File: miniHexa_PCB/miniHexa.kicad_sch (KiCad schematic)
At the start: 22 parts, among them SW1 SW_Push, U1 STM32F401RETx, Y2 25mhz

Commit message: start of version 2.0
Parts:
- removed R2: 0, Resistor_SMD:R_0603_1608Metric, symbol Device:R
- added U7: LSM6DS3, Package_LGA:LGA-14_3x2.5mm_P0.5mm_LayoutBorder3x4y, symbol Sensor_Motion:LSM6DS3
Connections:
- net +3.3V: now also U7.12 (CS), U7.5 (VDDIO), U7.8 (VDD)
- net GND: now also U7.1 (SDO/SA0), U7.2 (SDX), U7.3 (SCX), U7.6 (GND), U7.7 (GND)
- net RX: now reaches U1.42 (PA9)
- net TX: now reaches U1.43 (PA10)
- net at U1.61 (PB8): now also U7.13 (SCL)
- net I2C_SCK: no longer names the net of U1.58 (PB6)
- net I2C_SDA: no longer names the net of U1.59 (PB7)
- net I2C_SDA: now also U7.14 (SDA)
- net SERVO17: no longer names the net of U1.26 (PB0)
- net SERVO18: no longer names the net of U1.27 (PB1)

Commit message: mega update
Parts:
- added C31, C32, C33: 100nF, Capacitor_SMD:C_0402_1005Metric, symbol Device:C
- added R2, R6: 10k, Resistor_SMD:R_0402_1005Metric, symbol Device:R
- added R7: 0, Resistor_SMD:R_0603_1608Metric, symbol Device:R
- added U8: ST67W611M1A6UTR, pro_lib:U_QFN32L_ST67W611M1_STM-L, symbol pro_lib:ST67W611M1A6UTR
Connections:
- net +3.3V: now also C31.2, C32.2, C33.2, R2.1, R6.1, U8.16 (VDD33), U8.17 (CHIP_EN), U8.25 (VDDIO), U8.9 (VDDIO)
- net GND: now also C31.1, C32.1, C33.1, U8.10 (GND), U8.15 (GND), U8.18 (GND), U8.26 (GND), U8.30 (GND), U8.32 (GND), U8.33 (GND), U8.34 (GND), U8.35 (GND), U8.36 (GND)
- net ST67_BOOT: now reaches U1.17 (PA3)
- net ST67_BOOT: now also U8.3 (BOOT)
- net SP_CLK: now reaches U1.21 (PA5)
- net SP_CLK: now also U8.28 (SP_CLK)
- net at U1.22 (PA6): now also R7.2
- net SPI_MOSI: now reaches U1.23 (PA7)
- net SPI_MOSI: now also U8.27 (SPI_MOSI)
- net SPI_CS: now reaches U1.33 (PB12)
- net SPI_CS: now also U8.24 (SPI_CS)
- net ST67_TX: now reaches U1.38 (PC7)
- net ST67_TX: now also U8.22 (UART_TX)
- net SPI_RDY: now reaches U1.39 (PC8)
- net SPI_RDY: now also U8.21 (SPI_RDY)
- net SERVO_RX: now reaches U1.58 (PB6)
- net SERVO_RX: now also R2.2
- net at U7.14 (SDA): now also U1.61 (PB8); no longer U1.59 (PB7)
- net at U7.13 (SCL): now also U1.62 (PB9); no longer U1.61 (PB8)
- net CHIPEN_MIC_L renamed ST67_RX
- net ST67_RX: now also U8.23 (UART_RX)
- net CHIPEN_MIC_R: no longer names the net of U1.25 (PC5)
- net RX: no longer names the net of U1.42 (PA9)
- net TX: no longer names the net of U1.43 (PA10)
- new net SERVO_TX: R6.2, U1.59 (PB7)
- new net SPI_MISO: R7.1, U8.29 (SPI_MISO)
- no-connect marks 1 -> 3
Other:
- moved on the sheet: U7

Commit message: routed
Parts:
- C31, C32, C33: footprint Capacitor_SMD:C_0402_1005Metric -> Capacitor_SMD:C_0805_2012Metric
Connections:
- net +3.3V: no longer U8.17 (CHIP_EN)
- net CHIP_EN: now reaches U1.41 (PA8)
- net CHIP_EN: now also U8.17 (CHIP_EN)
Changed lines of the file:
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@@
 		)
 	)
+	(global_label "CHIP_EN"
+		(shape input)
+		(at 120.65 59.69 0)
+		(fields_autoplaced yes)
+		(effects
+			(font
+				(size 1.27 1.27)
+			)
+			(justify left)
+		)
+		(property "Intersheetrefs" "${INTERSHEET_REFS}"
+			(at 131.5576 59.69 0)
+			(hide yes)
+			(show_name no)
+			(do_not_autoplace no)
+			(effects
+				(font
+					(size 1.27 1.27)
+				)
+				(justify left)
+			)
+		)
+	)
 	(global_label "SPI_RDY"
 		(shape input)
@@
 		)
 	)
+	(global_label "CHIP_EN"
+		(shape input)
+		(at 175.26 71.12 180)
+		(fields_autoplaced yes)
+		(effects
+			(font
+				(size 1.27 1.27)
+			)
+			(justify right)
+		)
+		(property "Intersheetrefs" "${INTERSHEET_REFS}"
+			(at 164.3524 71.12 0)
+			(hide yes)
+			(show_name no)
+			(do_not_autoplace no)
+			(effects
+				(font
+					(size 1.27 1.27)
+				)
+				(justify right)
+			)
+		)
+	)
 	(symbol
 		(lib_id "power:GND")
@@
 		(lib_id "Device:C")
 		(at 261.62 54.61 0)
+		(mirror y)
 		(unit 1)
 		(body_style 1)
@@
 		(dnp no)
 		(property "Reference" "C33"
-			(at 253.746 50.038 0)
+			(at 269.494 50.038 0)
 			(show_name no)
 			(do_not_autoplace no)
@@
 		)
 		(property "Value" "100nF"
-			(at 253.746 52.578 0)
+			(at 269.494 52.578 0)
 			(show_name no)
 			(do_not_autoplace no)
@@
 			)
 		)
-		(property "Footprint" "Capacitor_SMD:C_0402_1005Metric"
-			(at 262.5852 58.42 0)
+		(property "Footprint" "Capacitor_SMD:C_0805_2012Metric"
+			(at 260.6548 58.42 0)
 			(hide yes)
 			(show_name no)
@@
 	)
 	(symbol
-		(lib_id "power:+3.3V")
-		(at 175.26 71.12 90)
-		(unit 1)
-		(body_style 1)
-		(exclude_from_sim no)
-		(in_bom yes)
-		(on_board yes)
-		(in_pos_files yes)
-		(dnp no)
-		(property "Reference" "#PWR069"
-			(at 179.07 71.12 0)
-			(hide yes)
-			(show_name no)
-			(do_not_autoplace no)
-			(effects
-				(font
-					(size 1.27 1.27)
-				)
-			)
-		)
-		(property "Value" "+3.3V"
-			(at 170.434 69.596 90)
-			(show_name no)
-			(do_not_autoplace no)
-			(effects
-				(font
-					(size 1.27 1.27)
-				)
-			)
-		)
-		(property "Footprint" ""
-			(at 175.26 71.12 0)
-			(hide yes)
-			(show_name no)
-			(do_not_autoplace no)
-			(effects
-				(font
-					(size 1.27 1.27)
-				)
-			)
-		)
-		(property "Datasheet" ""
-			(at 175.26 71.12 0)
-			(hide yes)
-			(show_name no)
-			(do_not_autoplace no)
-			(effects
-				(font
-					(size 1.27 1.27)
-				)
-			)
-		)
-		(property "Description" "Power symbol creates a global label with name \"+3.3V\""
-			(at 175.26 71.12 0)
-			(hide yes)
-			(show_name no)
-			(do_not_autoplace no)
-			(effects
-				(font
-					(size 1.27 1.27)
-				)
-			)
-		)
-		(pin "1"
-		)
-		(instances
-			(project "miniHexa"
-				(path "/3449ee66-2977-4802-a474-0821cdf4e79b"
-					(reference "#PWR069")
-					(unit 1)
-				)
-			)
-		)
-	)
-	(symbol
 		(lib_id "Device:C")
 		(at 52.07 24.13 0)
@@
 			)
 		)
-		(property "Footprint" "Capacitor_SMD:C_0402_1005Metric"
+		(property "Footprint" "Capacitor_SMD:C_0805_2012Metric"
 			(at 160.9852 68.58 0)
 			(hide yes)
@@
 			)
 		)
-		(property "Footprint" "Capacitor_SMD:C_0402_1005Metric"
+		(property "Footprint" "Capacitor_SMD:C_0805_2012Metric"
 			(at 167.3352 50.8 0)
 			(hide yes)

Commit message: update
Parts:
- added C34, C35: 100nF, Capacitor_SMD:C_0402_1005Metric, symbol Device:C
- added R8, R9: 4.7k, Resistor_SMD:R_0402_1005Metric, symbol Device:R
- U7: value LSM6DS3 -> LSM6DSL
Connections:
- net +3.3V: now also C34.2, C35.2, R8.2, R9.2
- net GND: now also C34.1, C35.1
- net IMU_INT1: now reaches U1.40 (PC9)
- net IMU_INT1: now also U7.4 (INT1)
- net at U1.61 (PB8): now also U7.13 (SCL), R8.1; no longer U7.14 (SDA)
- net at U1.62 (PB9): now also U7.14 (SDA), R9.1; no longer U7.13 (SCL)

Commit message: fixed RESET button issue
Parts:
- C1: value 20uF -> 2.2uF
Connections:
- net GND: now also C13.1, SW1.1; no longer C13.2
- net NRST: now reaches R1.1
- net NRST: now also C13.2, SW1.2, U1.7 (NRST); no longer SW1.1
- net SWDIO: now reaches U1.46 (PA13)
- net SWCLK: now reaches U1.49 (PA14)
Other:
- note added: "RESET BUTTON"
- moved on the sheet: C28, C29, R3

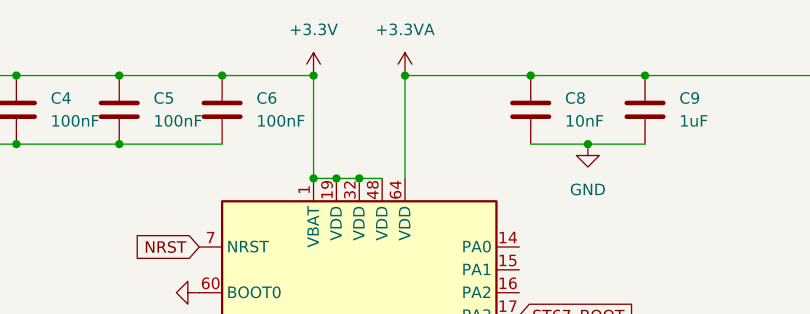
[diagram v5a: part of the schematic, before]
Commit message: updated some power lines
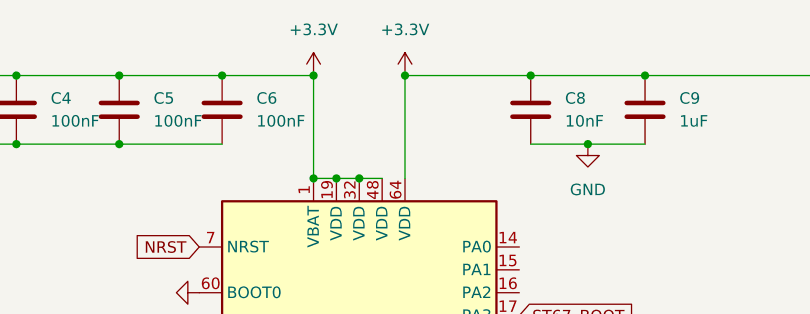
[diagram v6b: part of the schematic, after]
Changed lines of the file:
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@@
 	)
 	(junction
-		(at 107.95 20.32)
-		(diameter 0)
-		(color 0 0 0 0)
-	)
-	(junction
 		(at 255.27 140.97)
 		(diameter 0)
@@
 	)
 	(junction
+		(at 107.95 20.32)
+		(diameter 0)
+		(color 0 0 0 0)
+	)
+	(junction
 		(at 133.35 100.33)
 		(diameter 0)
@@
 	)
 	(symbol
-		(lib_id "power:+3.3VA")
-		(at 107.95 20.32 0)
-		(unit 1)
-		(body_style 1)
-		(exclude_from_sim no)
-		(in_bom yes)
-		(on_board yes)
-		(in_pos_files yes)
-		(dnp no)
-		(fields_autoplaced yes)
-		(property "Reference" "#PWR016"
-			(at 107.95 24.13 0)
-			(hide yes)
-			(show_name no)
-			(do_not_autoplace no)
-			(effects
-				(font
-					(size 1.27 1.27)
-				)
-			)
-		)
-		(property "Value" "+3.3VA"
-			(at 107.95 15.24 0)
-			(show_name no)
-			(do_not_autoplace no)
-			(effects
-				(font
-					(size 1.27 1.27)
-				)
-			)
-		)
-		(property "Footprint" ""
-			(at 107.95 20.32 0)
-			(hide yes)
-			(show_name no)
-			(do_not_autoplace no)
-			(effects
-				(font
-					(size 1.27 1.27)
-				)
-			)
-		)
-		(property "Datasheet" ""
-			(at 107.95 20.32 0)
-			(hide yes)
-			(show_name no)
-			(do_not_autoplace no)
-			(effects
-				(font
-					(size 1.27 1.27)
-				)
-			)
-		)
-		(property "Description" "Power symbol creates a global label with name \"+3.3VA\""
-			(at 107.95 20.32 0)
-			(hide yes)
-			(show_name no)
-			(do_not_autoplace no)
-			(effects
-				(font
-					(size 1.27 1.27)
-				)
-			)
-		)
-		(pin "1"
-		)
-		(instances
-			(project "miniHexa"
-				(path "/3449ee66-2977-4802-a474-0821cdf4e79b"
-					(reference "#PWR016")
-					(unit 1)
-				)
-			)
-		)
-	)
-	(symbol
 		(lib_id "Device:C")
 		(at 223.52 88.9 180)
@@
 					(unit 1)
 				)
+			)
+		)
+	)
+	(symbol
+		(lib_id "power:+3.3V")
+		(at 107.95 20.32 0)
+		(unit 1)
+		(body_style 1)
+		(exclude_from_sim no)
+		(in_bom yes)
+		(on_board yes)
+		(in_pos_files yes)
+		(dnp no)
+		(fields_autoplaced yes)
+		(property "Reference" "#PWR016"
+			(at 107.95 24.13 0)
+			(hide yes)
+			(show_name no)
+			(do_not_autoplace no)
+			(effects
+				(font
+					(size 1.27 1.27)
+				)
+			)
+		)
+		(property "Value" "+3.3V"
+			(at 107.95 15.24 0)
+			(show_name no)
+			(do_not_autoplace no)
+			(effects
+				(font
+					(size 1.27 1.27)
+				)
+			)
+		)
+		(property "Footprint" ""
+			(at 107.95 20.32 0)
+			(hide yes)
+			(show_name no)
+			(do_not_autoplace no)
+			(effects
+				(font
+					(size 1.27 1.27)
+				)
+			)
+		)
+		(property "Datasheet" ""
+			(at 107.95 20.32 0)
+			(hide yes)
+			(show_name no)
+			(do_not_autoplace no)
+			(effects
+				(font
+					(size 1.27 1.27)
+				)
+			)
+		)
+		(property "Description" "Power symbol creates a global label with name \"+3.3V\""
+			(at 107.95 20.32 0)
+			(hide yes)
+			(show_name no)
+			(do_not_autoplace no)
+			(effects
+				(font
+					(size 1.27 1.27)
+				)
+			)
+		)
+		(pin "1"
+		)
+		(instances
+			(project "miniHexa"
+				(path "/3449ee66-2977-4802-a474-0821cdf4e79b"
+					(reference "#PWR016")
+					(unit 1)
+				)

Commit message: tried to make it cleaner
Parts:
- removed R3: 0, Resistor_SMD:R_0603_1608Metric, symbol Device:R
- added JP1: 0hm, Resistor_SMD:R_0603_1608Metric, symbol Jumper:Jumper_2_Bridged
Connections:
- net MIC_SCK: now also JP1.1 (A), JP1.2 (B)
- no-connect marks 3 -> 12
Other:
- moved on the sheet: C34, C35, R32, R8, R9

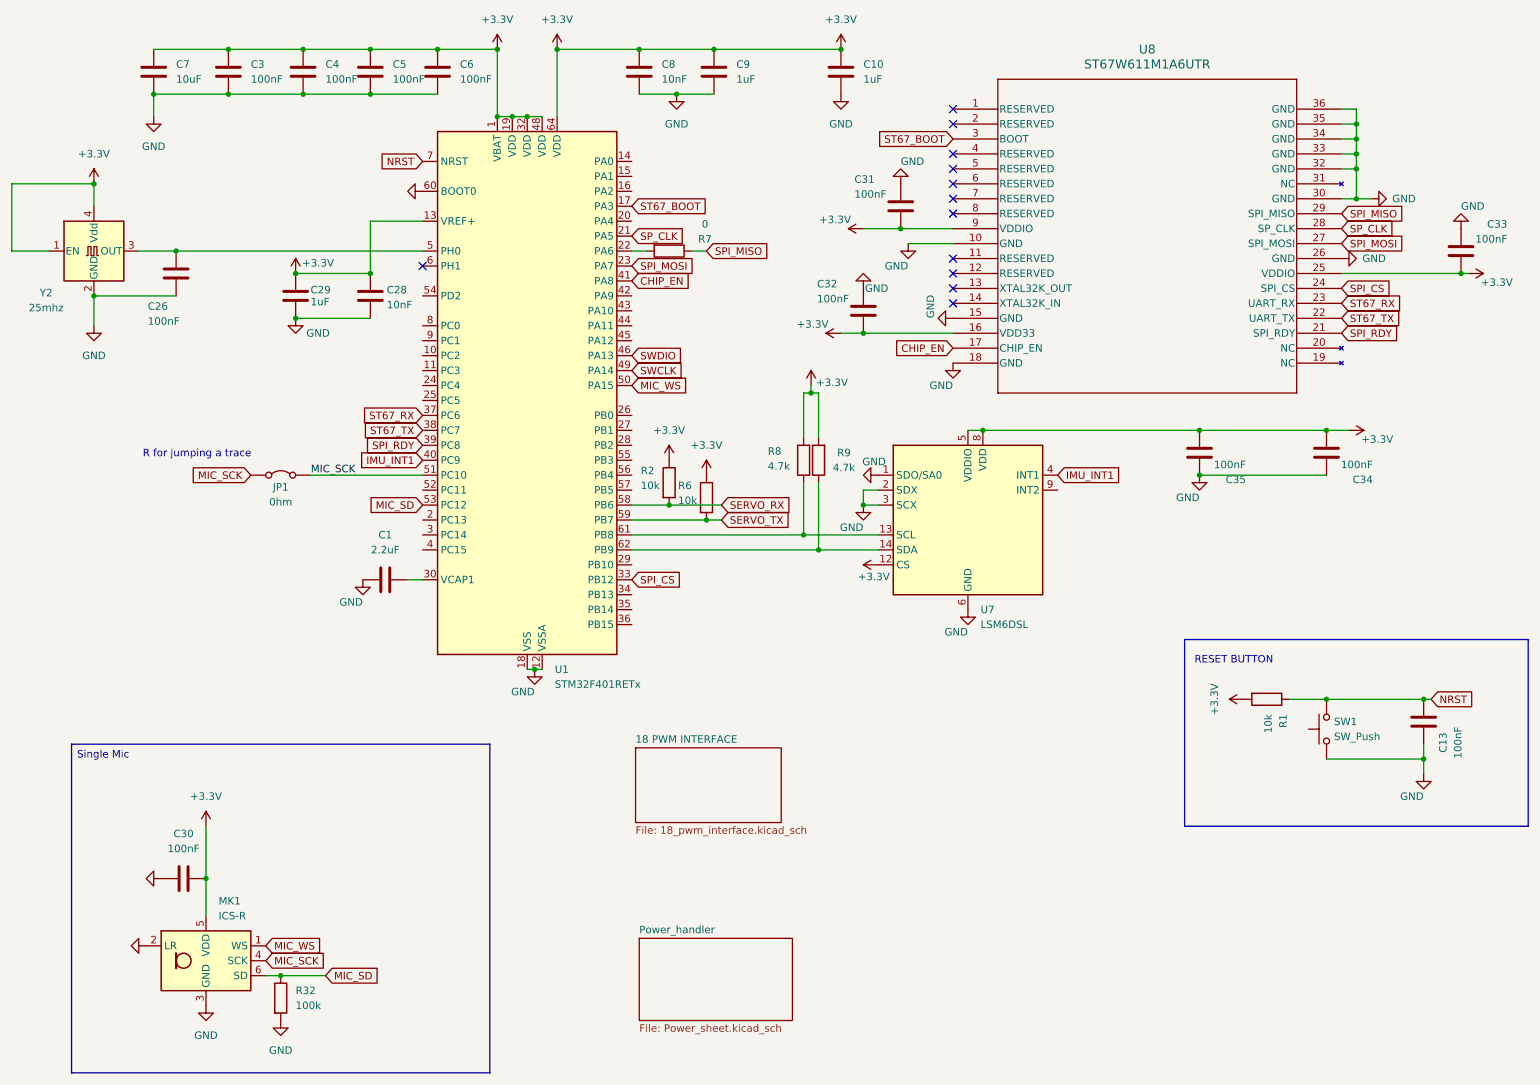
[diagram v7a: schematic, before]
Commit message: cleaned up; no major DRC violation
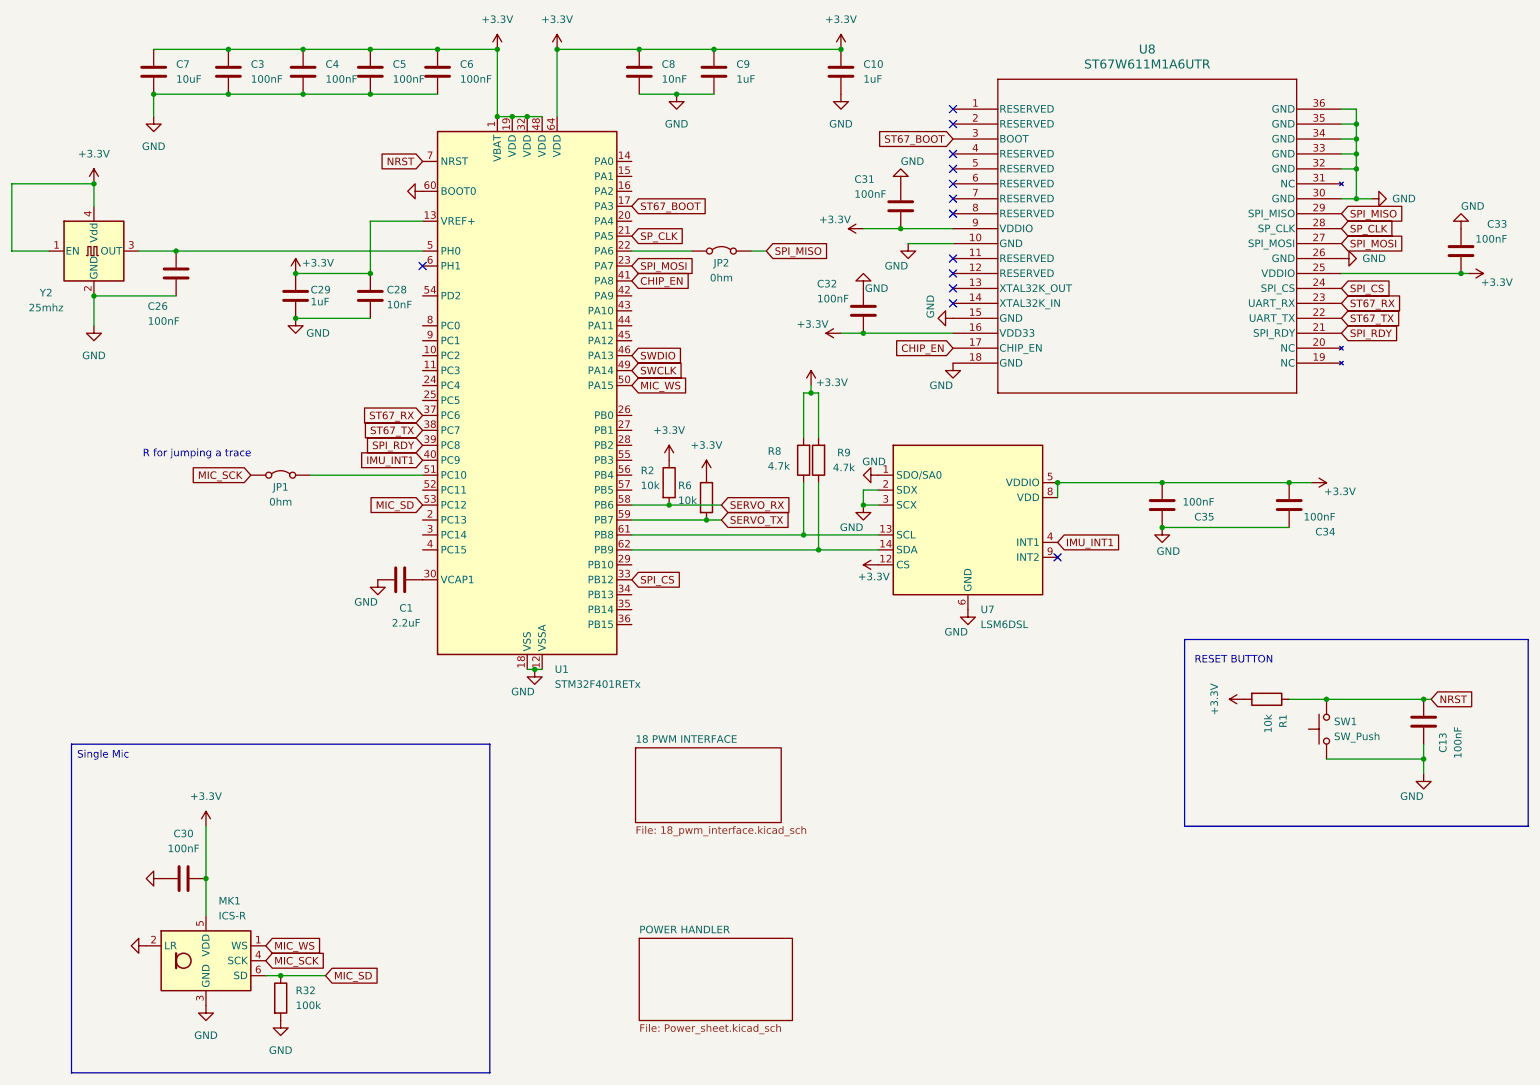
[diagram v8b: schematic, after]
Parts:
- removed R7: 0, Resistor_SMD:R_0603_1608Metric, symbol Device:R
- added JP2: 0hm, Resistor_SMD:R_0603_1608Metric, symbol Jumper:Jumper_2_Bridged
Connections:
- net MIC_SCK: no longer JP1.2 (B), U1.51 (PC10)
- net SPI_MISO: now also JP2.2 (B)
- net at U1.22 (PA6): now also JP2.1 (A)
- new net: JP1.2 (B), U1.51 (PC10)
- no-connect marks 12 -> 13
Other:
- sheet Power_handler renamed POWER HANDLER
- moved on the sheet: C1, C34, C35, U7
